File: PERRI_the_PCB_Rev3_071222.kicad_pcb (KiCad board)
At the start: 2 copper layers, 163 x 100 mm, 42 parts, among them J1 SS5-80-3.00-X-D-K-XX, J2 Conn_01x02, J3 Conn_02x50_Counter_Clockwise, J4 Conn_02x05_Counter_Clockwise, J5 SS5-80-3.00-X-D-K-XX, J6 Conn_01x03, J7 Conn_01x03, J8 Conn_01x03, SW2 SW_DIP_x08, U1 TMP441AIDCNR, U2 TPS2595, U3 PCA9554ADB, U4 NCV8508

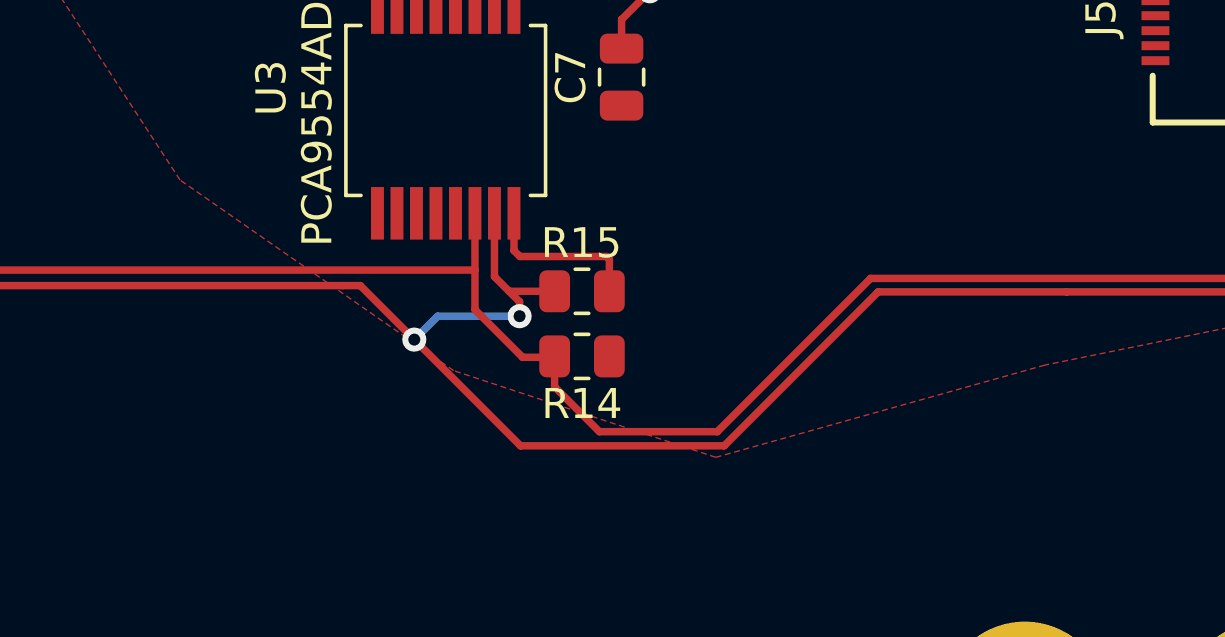
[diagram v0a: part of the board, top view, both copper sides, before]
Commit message: Fixed some alignment issues
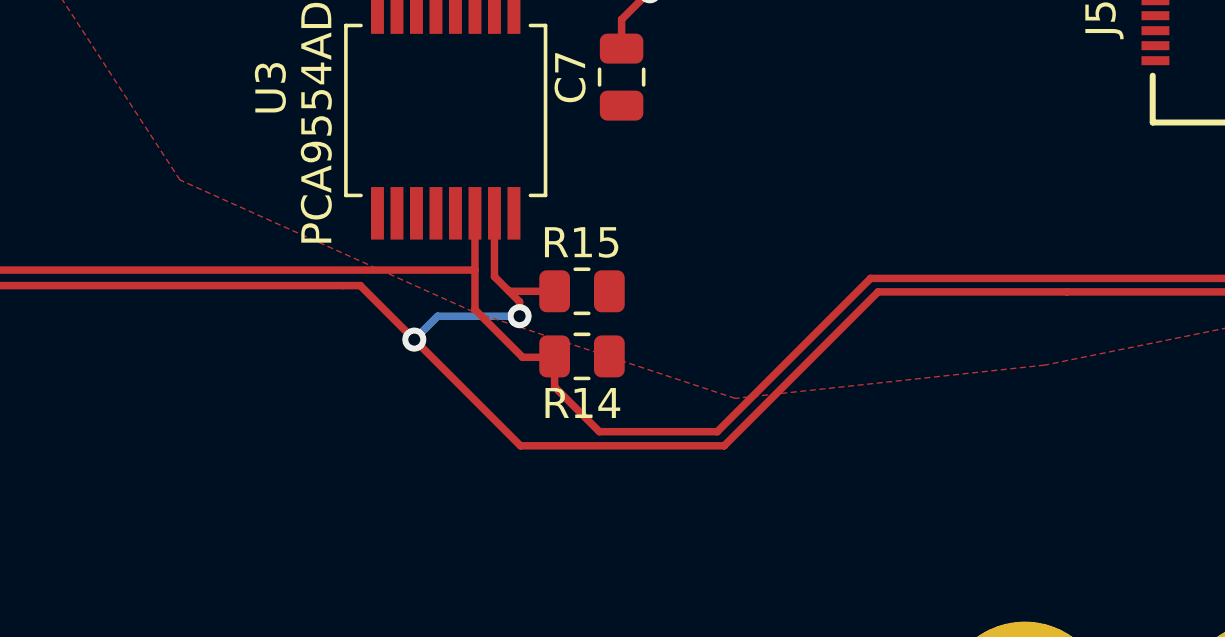
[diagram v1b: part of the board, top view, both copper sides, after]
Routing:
- net +5V: track 8.24 -> 2.63 mm
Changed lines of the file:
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@@
   (segment (start 131.320801 67.389199) (end 131.3 67.41) (width 0.25) (layer "F.Cu") (net 8))
   (segment (start 130.88 67.42) (end 130.88 68.64) (width 0.25) (layer "F.Cu") (net 8))
-  (segment (start 137.74 122.51) (end 137.8325 122.6025) (width 0.25) (layer "F.Cu") (net 8))
-  (segment (start 137.8325 122.6025) (end 137.8325 123.67) (width 0.25) (layer "F.Cu") (net 8))
   (segment (start 130.89 67.41) (end 130.88 67.42) (width 0.25) (layer "F.Cu") (net 8))
-  (segment (start 134.85 122.51) (end 137.74 122.51) (width 0.25) (layer "F.Cu") (net 8))
-  (segment (start 134.652499 122.312499) (end 134.85 122.51) (width 0.25) (layer "F.Cu") (net 8))
-  (segment (start 134.652499 121.07095) (end 134.652499 122.312499) (width 0.25) (layer "F.Cu") (net 8))
   (segment (start 148.23 74.81) (end 149.903 76.483) (width 0.2) (layer "F.Cu") (net 9))
   (segment (start 148.23 71.62) (end 148.23 74.81) (width 0.2) (layer "F.Cu") (net 9))
@@
         (xy 164.09 123.73)
         (xy 152.35 126.13)
-        (xy 141.380622 129.203868)
-        (xy 132.640622 126.313868)
+        (xy 142.03 127.24)
+        (xy 133.29 124.35)
         (xy 123.52 119.96)
         (xy 117.83 111.24)

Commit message: Ready for Fab
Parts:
- added G***: LOGO, footprints:OSU_Logo, F.Cu at (106.7, 66.7)
- added G***: LOGO, footprints:PUEO150, F.Cu at (167.0, 93.4)
- added G***: LOGO, footprints:Perry, F.Cu at (113.8, 67.7)
- J2: value Conn_01x02 -> External power
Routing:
- net /DXP: track 13.0 -> 19.8 mm
- net /DXN: track 17.6 -> 23.7 mm
- net GND: track 256.2 -> 257.7 mm
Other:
- board text added: "P. Linton PERRI REV1 07/13/2022"
